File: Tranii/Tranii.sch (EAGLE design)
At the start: 26 parts

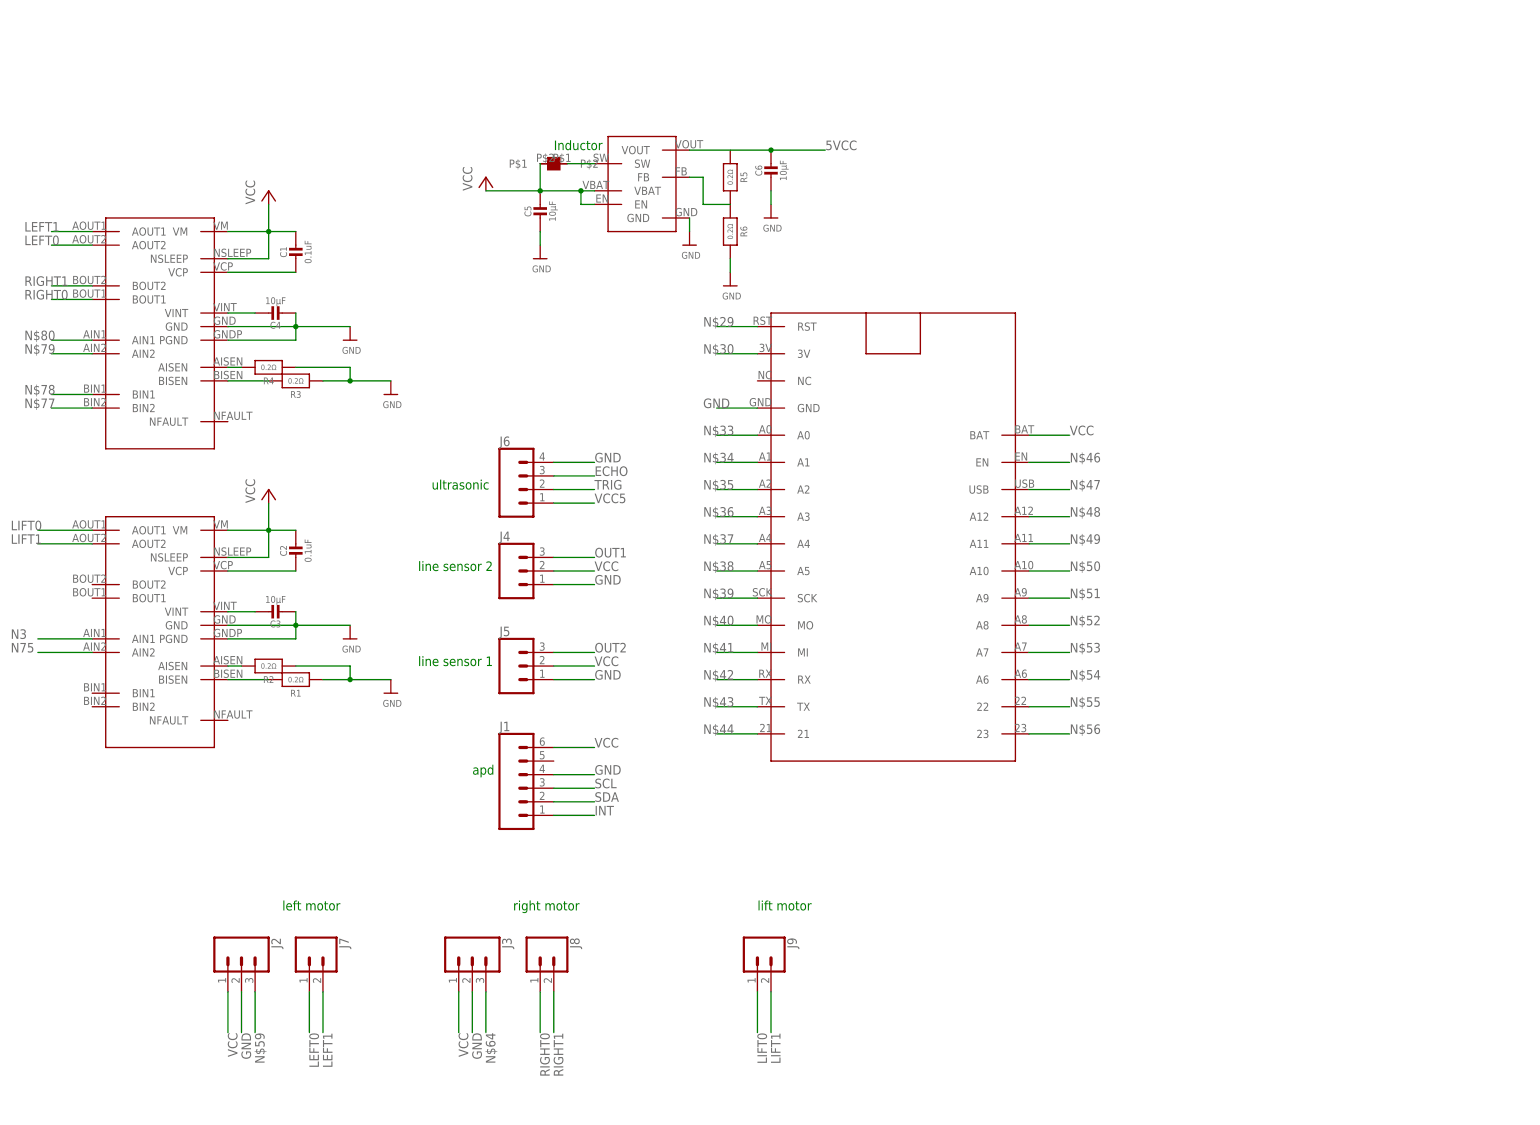
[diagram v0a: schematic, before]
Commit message: finished pin mapping
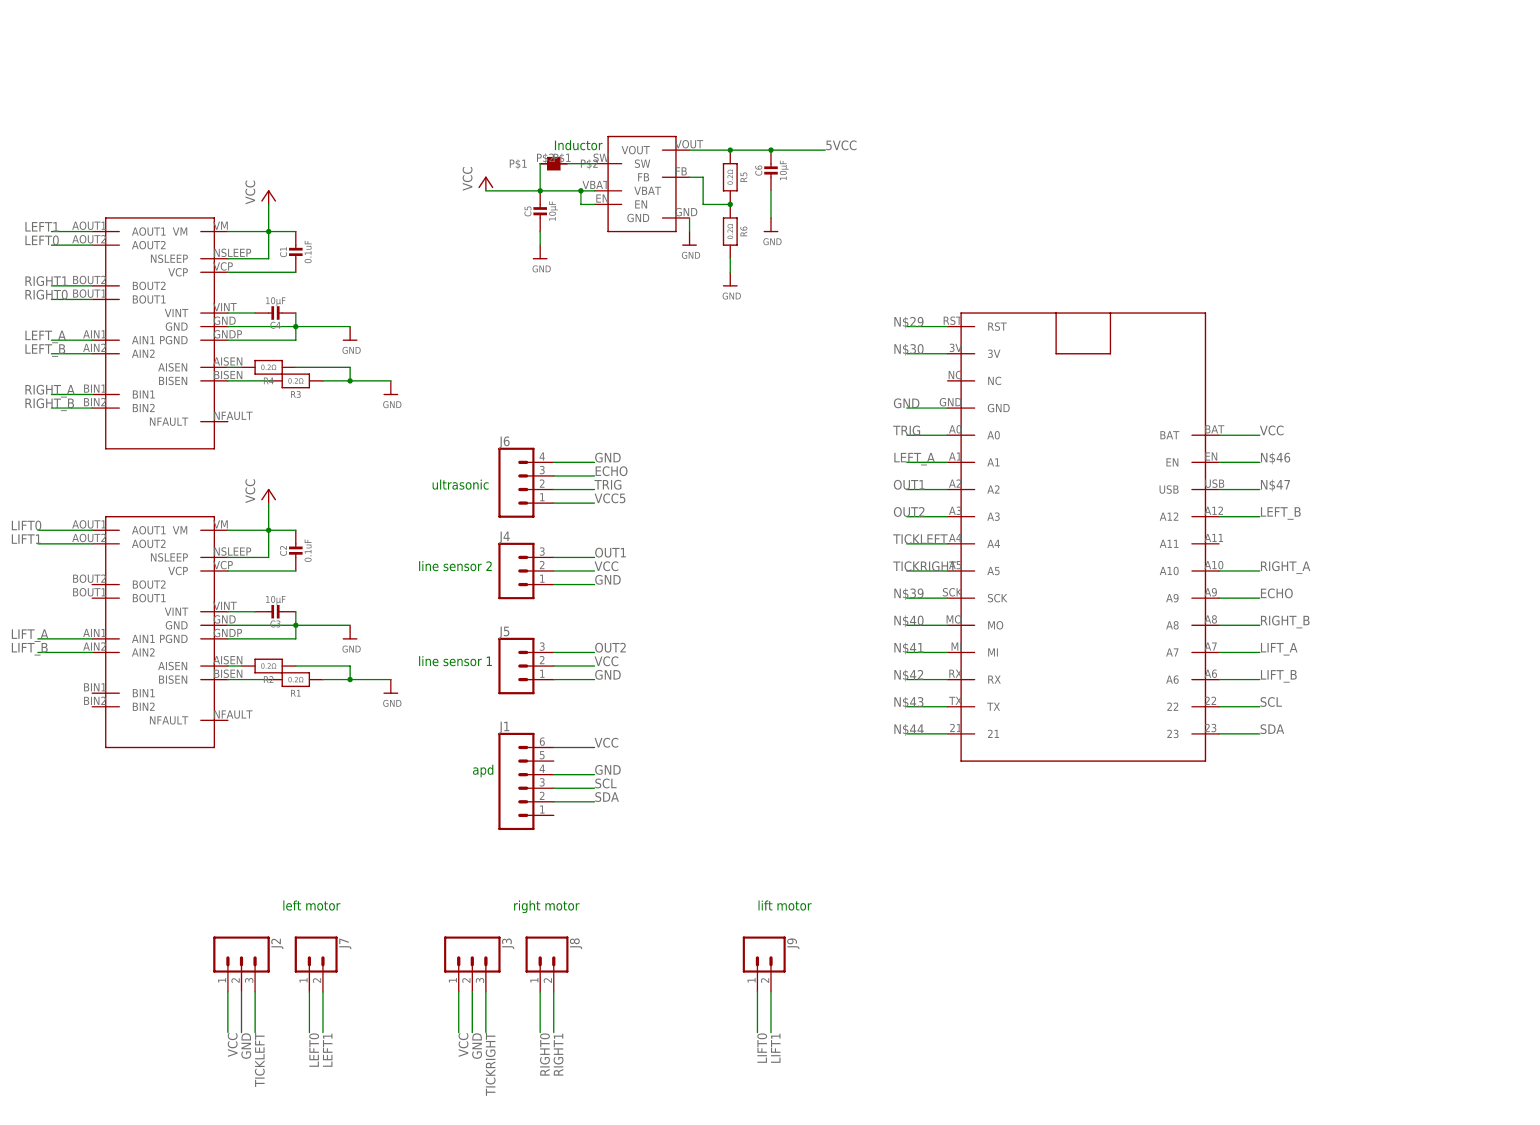
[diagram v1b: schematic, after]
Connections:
- removed net INT: J1.1
- removed net N$33: U$6.A0
- removed net N$34: U$6.A1
- removed net N$35: U$6.A2
- removed net N$36: U$6.A3
- removed net N$37: U$6.A4
- removed net N$38: U$6.A5
- removed net N$48: U$6.A12
- removed net N$49: U$6.A11
- removed net N$50: U$6.A10
- removed net N$51: U$6.A9
- removed net N$52: U$6.A8
- removed net N$53: U$6.A7
- removed net N$54: U$6.A6
- removed net N$55: U$6.22
- removed net N$56: U$6.23
- removed net N$59: J2.3
- removed net N$64: J3.3
- removed net N$77: U$1.BIN2
- removed net N$78: U$1.BIN1
- removed net N$79: U$1.AIN2
- removed net N$80: U$1.AIN1
- removed net N3: U$2.AIN1
- removed net N75: U$2.AIN2
- new net LEFT_A: U$1.AIN1, U$6.A1
- new net LEFT_B: U$1.AIN2, U$6.A12
- new net LIFT_A: U$2.AIN1, U$6.A7
- new net LIFT_B: U$2.AIN2, U$6.A6
- new net RIGHT_A: U$1.BIN1, U$6.A10
- new net RIGHT_B: U$1.BIN2, U$6.A8
- new net TICKLEFT: J2.3, U$6.A4
- new net TICKRIGHT: J3.3, U$6.A5
- net 5VCC: now also R5.1
- net ECHO: now also U$6.A9
- net N$1: now also R6.1
- net OUT1: now also U$6.A2
- net OUT2: now also U$6.A3
- net SCL: now also U$6.22
- net SDA: now also U$6.23
- net TRIG: now also U$6.A0

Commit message: cleaned up schematic
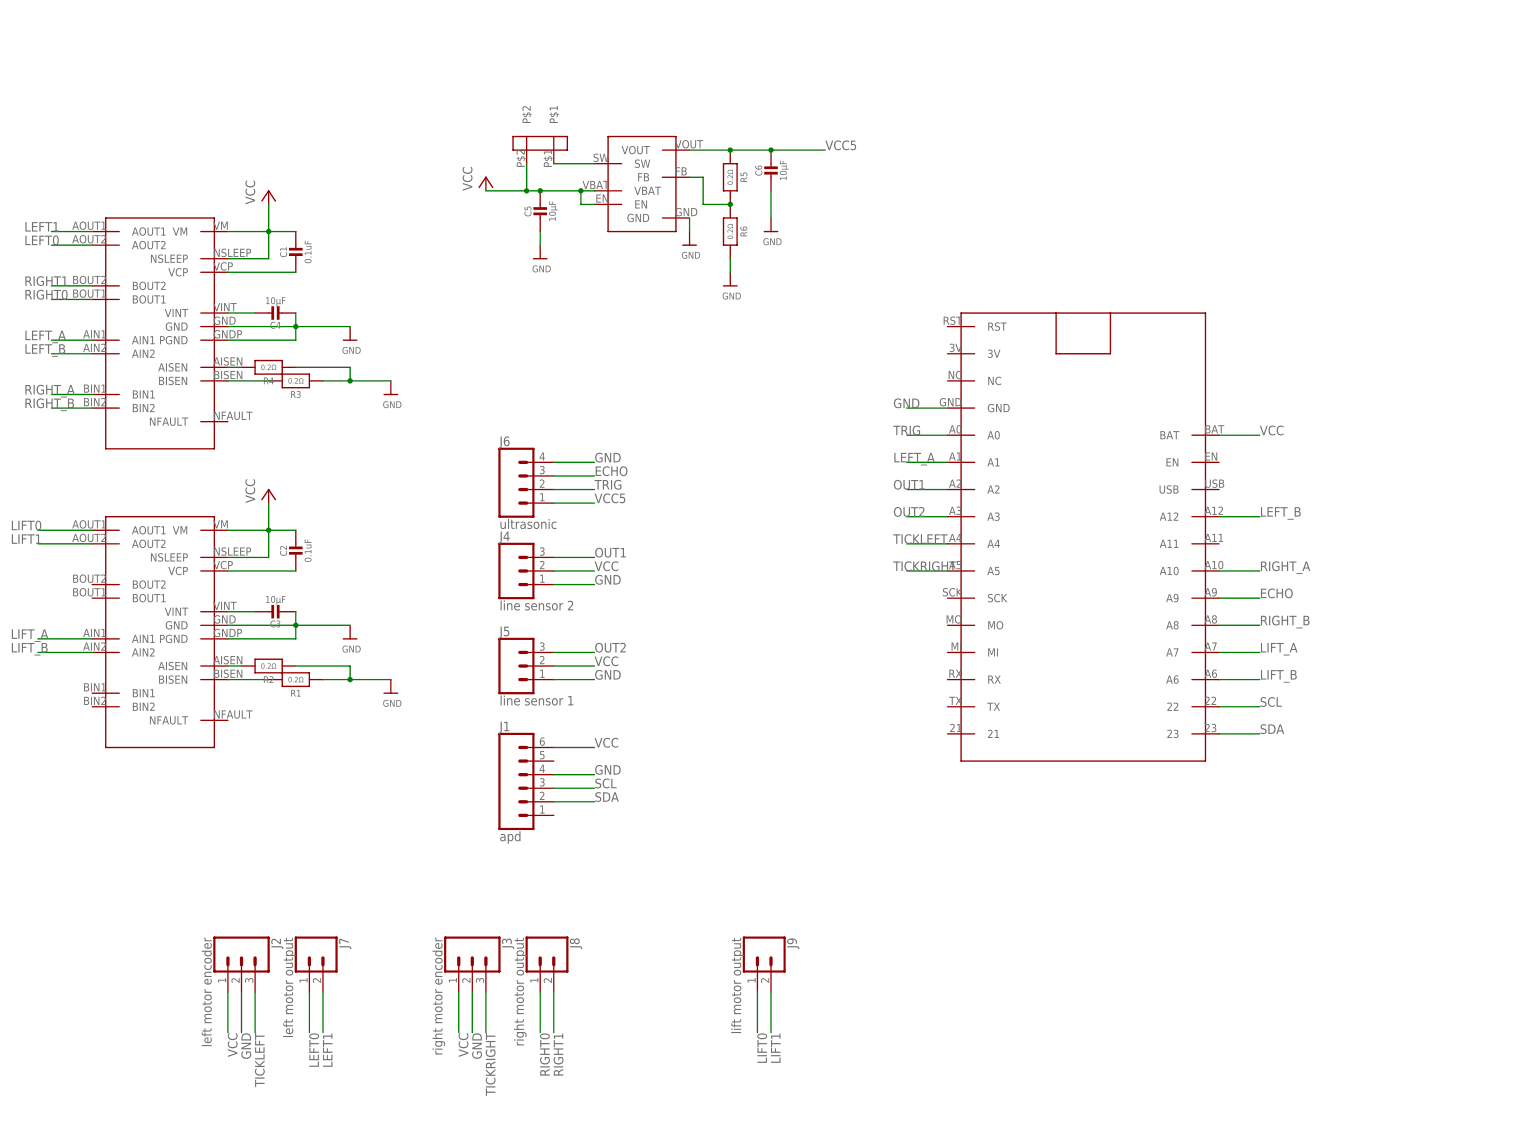
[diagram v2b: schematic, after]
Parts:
- J1: value (none) -> apd
- J2: value (none) -> left motor encoder
- J3: value (none) -> right motor encoder
- J4: value (none) -> line sensor 2
- J5: value (none) -> line sensor 1
- J6: value (none) -> ultrasonic
- J7: value (none) -> left motor output
- J8: value (none) -> right motor output
- J9: value (none) -> lift motor output
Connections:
- removed net 5VCC: C6.1, R5.1, U$8.VOUT
- removed net N$2 (its old number): U$8.GND
- removed net N$29: U$6.RST
- removed net N$30: U$6.3V
- removed net N$39: U$6.SCK
- removed net N$40: U$6.MO
- removed net N$41: U$6.MI
- removed net N$42: U$6.RX
- removed net N$43: U$6.TX
- removed net N$44: U$6.21
- removed net N$46: U$6.EN
- removed net N$47: U$6.USB
- net GND: now also U$8.GND
- net VCC5: now also C6.1, R5.1, U$8.VOUT
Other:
- note removed: "Inductor"
- note removed: "apd"
- note removed: "left motor"
- note removed: "lift motor"
- note removed: "line sensor 1"
- note removed: "line sensor 2"
- note removed: "right motor"
- note removed: "ultrasonic"

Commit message: finished schematic
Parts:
- removed U$11: VLS3012HBX, Tranii:VLS3012HBX
- added R7: 47Ω, microbuilder:RESISTOR_1206
- added R8: 91Ω, microbuilder:RESISTOR_1206
- added U$12: VLS3012HBX, Tranii:VLS3012HBX
- added U$9: LM3671, Tranii:LM3671
- C5: value 10µF -> 4.7uF
- C6: value 10µF -> 10uF
- R5, R6: value 0.2Ω -> 10kΩ
- U$8: value LPV61220 -> BSS138; device Tranii:LPV61220 -> Tranii:BSS138
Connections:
- new net 3V: J2.1, J3.1, J4.2, J5.2, U$6.3V
- new net ECHO3.3: R7.2, R8.1, U$6.A9
- new net TRIG3.3: R5.2, U$6.A0, U$8.S
- net ECHO: now also R7.1; no longer U$6.A9
- net GND: now also R8.2, U$9.GND; no longer R6.2, U$8.GND
- net N$1: now also U$12.P$1, U$9.SW; no longer R5.2, R6.1, U$8.FB
- net N$2: now also C6.1, U$12.P$2, U$9.FB; no longer U$11.P$1, U$8.SW
- net TRIG: now also R6.2, U$8.D; no longer U$6.A0
- net VCC: now also R5.1, U$8.G, U$9.EN, U$9.VIN; no longer J2.1, J3.1, J4.2, J5.2, U$11.P$2, U$8.EN, U$8.VBAT
- net VCC5: now also R6.1; no longer C6.1, R5.1, U$8.VOUT
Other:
- moved on the sheet: C5, C6, R5, R6
